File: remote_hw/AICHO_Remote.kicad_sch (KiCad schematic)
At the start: 25 parts, among them J1 Conn_01x04, J2 Conn_01x03_Pin, J3 RJ45, U1 TPS54302, U3 PY32F003F18U6, U4 SP485E, Y1 16MHz 9pF

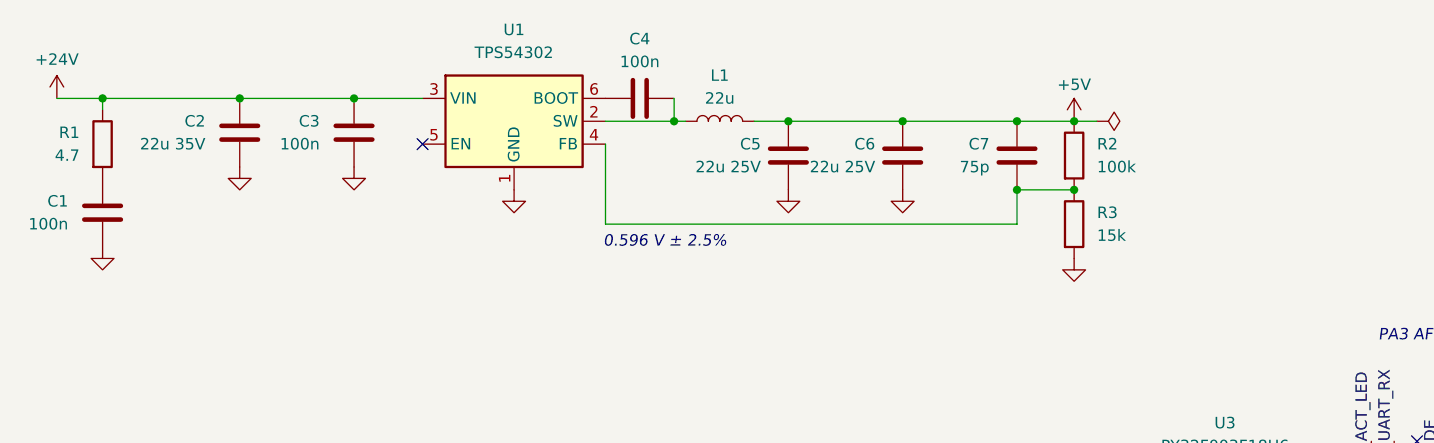
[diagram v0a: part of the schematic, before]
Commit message: remote_hw: Change DC-DC input capacitors to 10 uF * 2
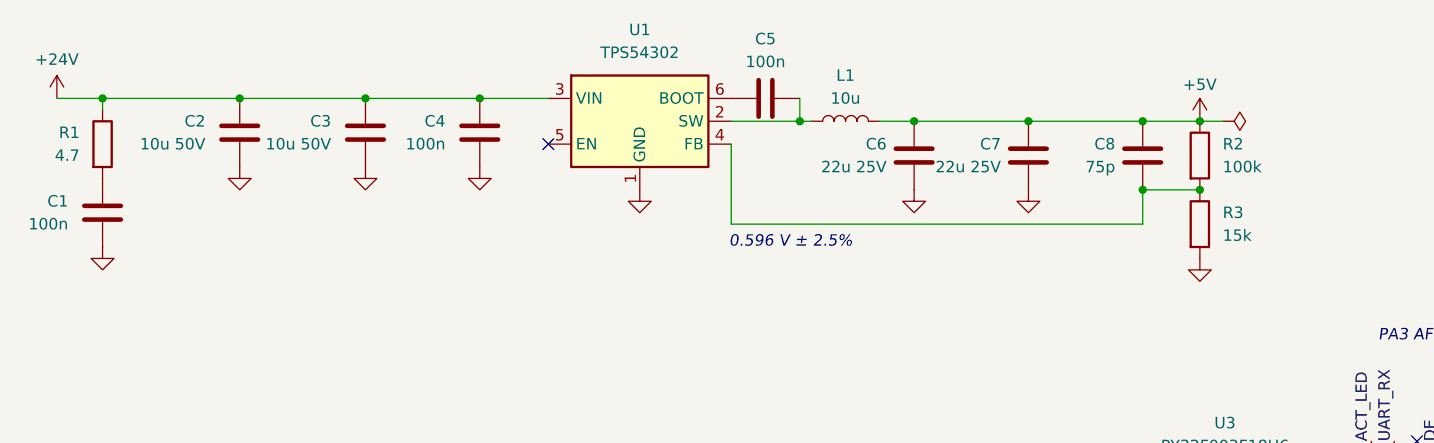
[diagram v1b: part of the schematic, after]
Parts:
- added C3: 10u 50V, Capacitor_SMD:C_0805_2012Metric, symbol Device:C
- C2: value 22u 35V -> 10u 50V; footprint Capacitor_SMD:C_1210_3225Metric -> Capacitor_SMD:C_0805_2012Metric; LCSC PN C778721 -> C338080; Mfr PN (none) -> C2012X5R1V226MT000E
- L1: value 22u -> 10u; footprint Inductor_SMD:L_Sunlord_SWPA6045S -> Inductor_SMD:L_Sunlord_SWPA4030S; LCSC PN C83454 -> C38117; Mfr PN SWPA6045S220MT -> SWPA4030S100MT
- renumbered C3 to C4, C4 to C5, C5 to C6, C6 to C7, C7 to C8
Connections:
- net +24V: now also C3.1
- net GND: now also C3.2
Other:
- moved on the sheet: C4, C5, C6, C7, C8, L1, R2, R3, U1

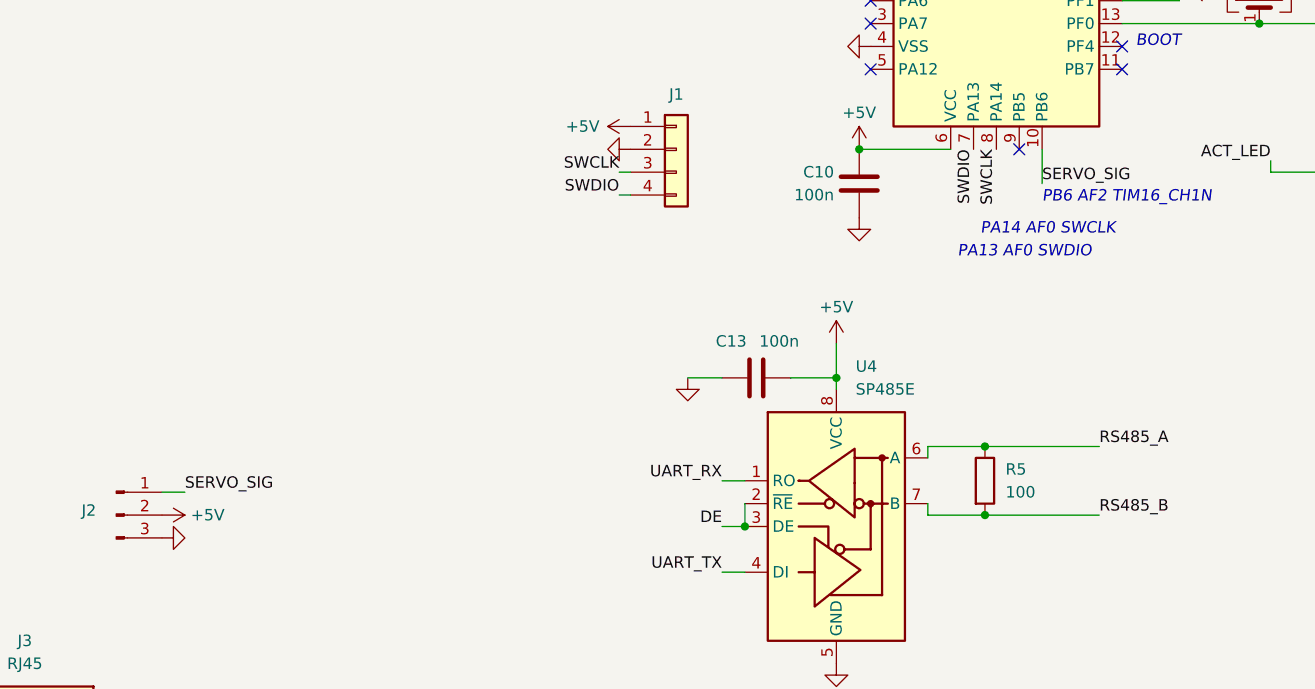
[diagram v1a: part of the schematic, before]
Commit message: remote_hw: Lay out DC-DC
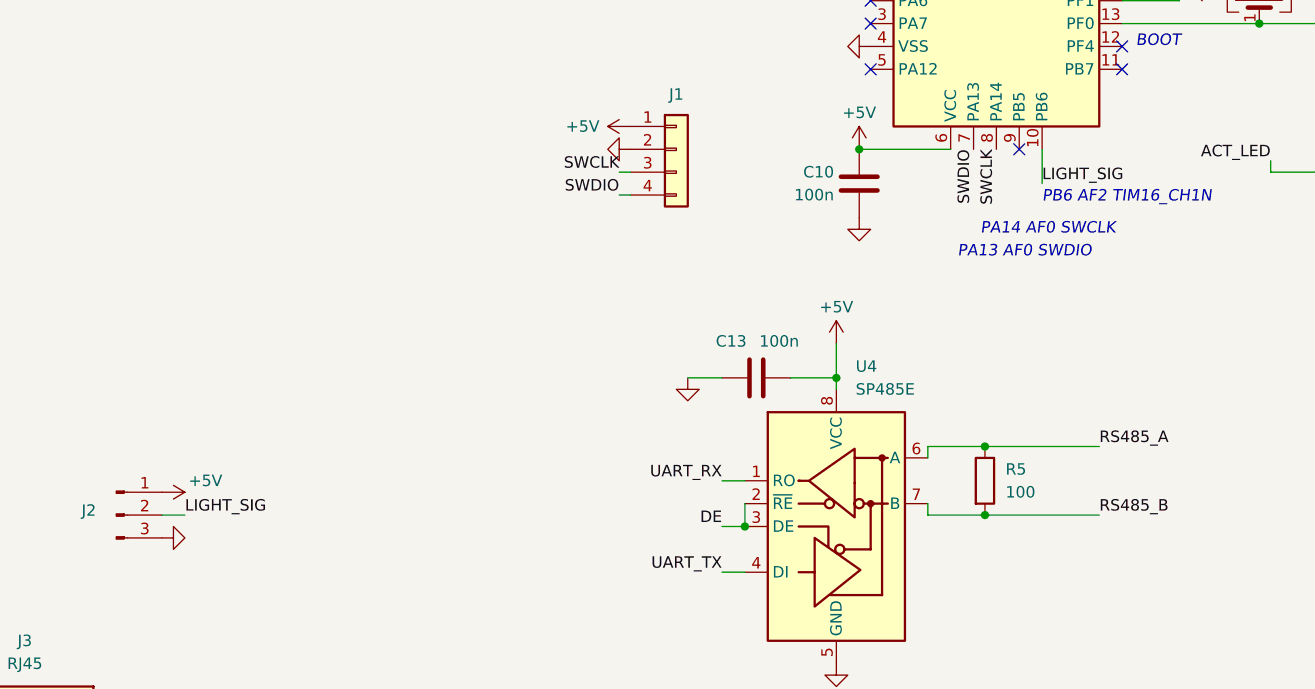
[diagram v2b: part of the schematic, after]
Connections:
- net +5V: now also J2.1 (Pin_1); no longer J2.2 (Pin_2)
- net SERVO_SIG renamed LIGHT_SIG
- net LIGHT_SIG: now also J2.2 (Pin_2); no longer J2.1 (Pin_1)
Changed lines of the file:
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@@
 	(wire
 		(pts
-			(xy 85.09 133.35) (xy 82.55 133.35)
+			(xy 85.09 135.89) (xy 82.55 135.89)
 		)
 		(stroke
@@
 		)
 	)
-	(label "SERVO_SIG"
-		(at 85.09 133.35 0)
+	(label "LIGHT_SIG"
+		(at 85.09 135.89 0)
 		(effects
 			(font
@@
 		)
 	)
-	(label "SERVO_SIG"
+	(label "LIGHT_SIG"
 		(at 180.34 99.06 0)
 		(effects
@@
 	(symbol
 		(lib_id "power:+5V")
-		(at 82.55 135.89 270)
+		(at 82.55 133.35 270)
 		(unit 1)
 		(exclude_from_sim no)
@@
 		(dnp no)
 		(property "Reference" "#PWR016"
-			(at 78.74 135.89 0)
+			(at 78.74 133.35 0)
 			(effects
 				(font
@@
 		)
 		(property "Value" "+5V"
-			(at 87.63 135.89 90)
+			(at 87.376 132.08 90)
 			(effects
 				(font
@@
 		)
 		(property "Footprint" ""
-			(at 82.55 135.89 0)
+			(at 82.55 133.35 0)
 			(effects
 				(font
@@
 		)
 		(property "Datasheet" ""
-			(at 82.55 135.89 0)
+			(at 82.55 133.35 0)
 			(effects
 				(font
@@
 		)
 		(property "Description" "Power symbol creates a global label with name \"+5V\""
-			(at 82.55 135.89 0)
-			(effects
-				(font
+			(at 82.55 133.35 0)
+			(effects
+				(font

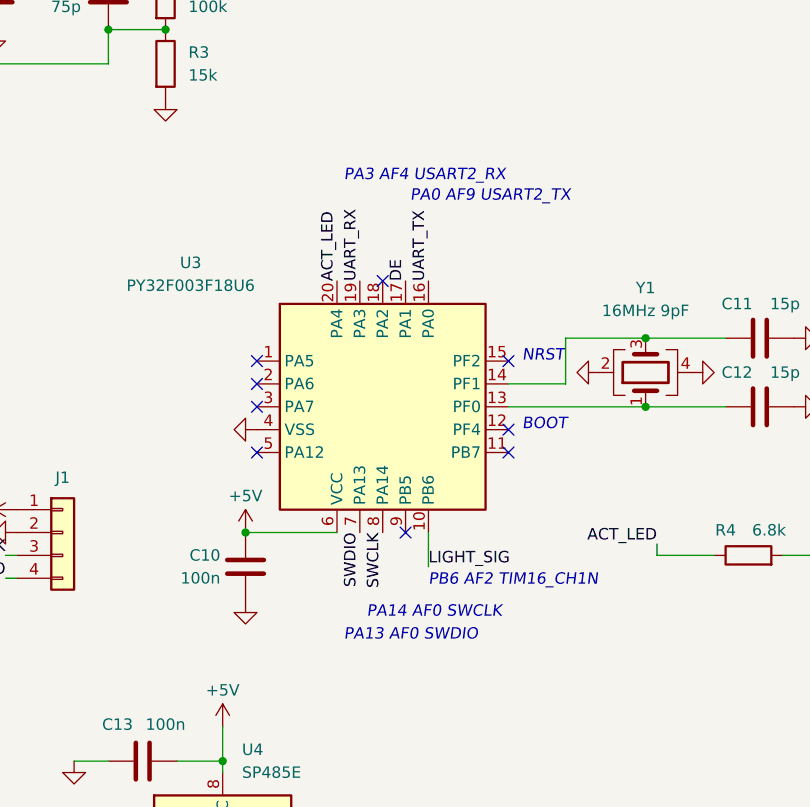
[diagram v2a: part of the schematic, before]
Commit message: remote_hw: Finish layout & routing
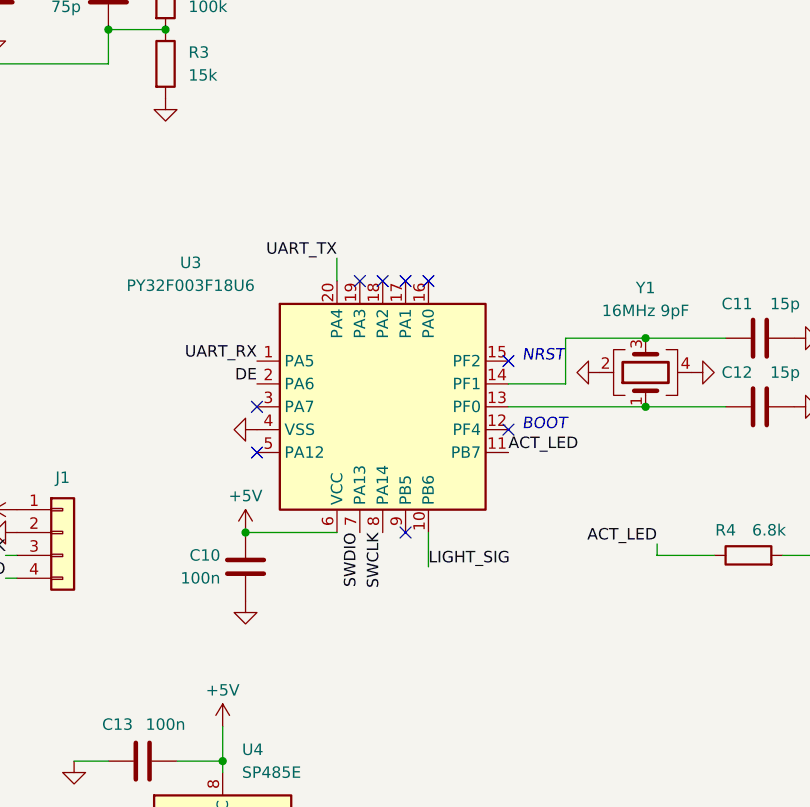
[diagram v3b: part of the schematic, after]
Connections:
- net ACT_LED: now also U3.11 (PB7); no longer U3.20 (PA4)
- net DE: now also U3.2 (PA6); no longer U3.17 (PA1)
- net UART_RX: now also U3.1 (PA5); no longer U3.19 (PA3)
- net UART_TX: now also U3.20 (PA4); no longer U3.16 (PA0)
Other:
- note removed: "PA0 AF9 USART2_TX"
- note removed: "PA13 AF0 SWDIO"
- note removed: "PA14 AF0 SWCLK"
- note removed: "PA3 AF4 USART2_RX"
- note removed: "PB6 AF2 TIM16_CH1N"
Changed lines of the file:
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@@
 	(generator_version "9.0")
 	(paper "A4")
-	(text "PA0 AF9 USART2_TX"
-		(exclude_from_sim no)
-		(at 178.308 58.674 0)
-		(effects
-			(font
-				(size 1.27 1.27)
-				(italic yes)
-			)
-			(justify left bottom)
-		)
-	)
 	(text "BOOT"
 		(exclude_from_sim no)
@@
 		)
 	)
-	(text "PA3 AF4 USART2_RX"
-		(exclude_from_sim no)
-		(at 170.942 56.388 0)
-		(effects
-			(font
-				(size 1.27 1.27)
-				(italic yes)
-			)
-			(justify left bottom)
-		)
-	)
 	(text "0.596 V ± 2.5%"
 		(exclude_from_sim no)
@@
 		)
 	)
-	(text "PA14 AF0 SWCLK"
-		(exclude_from_sim no)
-		(at 173.482 104.902 0)
-		(effects
-			(font
-				(size 1.27 1.27)
-				(italic yes)
-			)
-			(justify left bottom)
-		)
-	)
-	(text "PA13 AF0 SWDIO"
-		(exclude_from_sim no)
-		(at 170.942 107.442 0)
-		(effects
-			(font
-				(size 1.27 1.27)
-				(italic yes)
-			)
-			(justify left bottom)
-		)
-	)
-	(text "PB6 AF2 TIM16_CH1N"
-		(exclude_from_sim no)
-		(at 180.34 101.346 0)
-		(effects
-			(font
-				(size 1.27 1.27)
-				(italic yes)
-			)
-			(justify left bottom)
-		)
-	)
 	(junction
 		(at 29.21 29.21)
@@
 	)
 	(no_connect
+		(at 177.8 67.31)
+	)
+	(no_connect
 		(at 161.29 86.36)
 	)
@@
 	)
 	(no_connect
-		(at 189.23 86.36)
-	)
-	(no_connect
-		(at 161.29 78.74)
-	)
-	(no_connect
 		(at 78.74 34.29)
 	)
 	(no_connect
-		(at 161.29 76.2)
-	)
-	(no_connect
 		(at 161.29 81.28)
 	)
@@
 		(at 189.23 83.82)
 	)
+	(no_connect
+		(at 180.34 67.31)
+	)
+	(no_connect
+		(at 172.72 67.31)
+	)
 	(wire
 		(pts
@@
 		(pts
 			(xy 219.71 97.79) (xy 223.52 97.79)
+		)
+		(stroke
+			(width 0)
+			(type default)
+		)
+	)
+	(wire
+		(pts
+			(xy 170.18 64.77) (xy 170.18 67.31)
 		)
 		(stroke
@@
 		)
 	)
-	(label "UART_RX"
-		(at 172.72 67.31 90)
-		(effects
-			(font
-				(size 1.27 1.27)
-			)
-			(justify left bottom)
-		)
-	)
 	(label "SWDIO"
 		(at 172.72 95.25 270)
@@
 		)
 	)
-	(label "UART_TX"
-		(at 180.34 67.31 90)
-		(effects
-			(font
-				(size 1.27 1.27)
-			)
-			(justify left bottom)
-		)
-	)
 	(label "SWDIO"
 		(at 133.35 100.33 180)
@@
 		)
 	)
+	(label "DE"
+		(at 161.29 78.74 180)
+		(effects
+			(font
+				(size 1.27 1.27)
+			)
+			(justify right bottom)
+		)
+	)
 	(label "ACT_LED"
 		(at 205.74 96.52 180)
@@
 		)
 	)
+	(label "ACT_LED"
+		(at 189.23 86.36 0)
+		(effects
+			(font
+				(size 1.27 1.27)
+			)
+			(justify left bottom)
+		)
+	)
+	(label "UART_RX"
+		(at 161.29 76.2 180)
+		(effects
+			(font
+				(size 1.27 1.27)
+			)
+			(justify right bottom)
+		)
+	)
+	(label "RS485_B"
+		(at 186.69 135.89 0)
+		(effects
+			(font
+				(size 1.27 1.27)
+			)
+			(justify left bottom)
+		)
+	)
+	(label "UART_TX"
+		(at 144.78 142.24 180)
+		(effects
+			(font
+				(size 1.27 1.27)
+			)
+			(justify right bottom)
+		)
+	)
+	(label "SWCLK"
+		(at 133.35 97.79 180)
+		(effects
+			(font
+				(size 1.27 1.27)
+			)
+			(justify right bottom)
+		)
+	)
+	(label "UART_TX"
+		(at 170.18 64.77 180)
+		(effects
+			(font
+				(size 1.27 1.27)
+			)
+			(justify right bottom)
+		)
+	)
+	(label "SWCLK"
+		(at 175.26 95.25 270)
+		(effects
+			(font
+				(size 1.27 1.27)
+			)
+			(justify right bottom)
+		)
+	)
+	(label "RS485_B"
+		(at 80.01 172.72 0)
+		(effects
+			(font
+				(size 1.27 1.27)
+			)
+			(justify left bottom)
+		)
+	)
 	(label "LIGHT_SIG"
 		(at 180.34 99.06 0)
 		(effects
 			(font
-				(size 1.27 1.27)
-			)
-			(justify left bottom)
-		)
-	)
-	(label "RS485_B"
-		(at 186.69 135.89 0)
-		(effects
-			(font
-				(size 1.27 1.27)
-			)
-			(justify left bottom)
-		)
-	)
-	(label "UART_TX"
-		(at 144.78 142.24 180)
-		(effects
-			(font
-				(size 1.27 1.27)
-			)
-			(justify right bottom)
-		)
-	)
-	(label "DE"
-		(at 177.8 67.31 90)
-		(effects
-			(font
-				(size 1.27 1.27)
-			)
-			(justify left bottom)
-		)
-	)
-	(label "ACT_LED"
-		(at 170.18 67.31 90)
-		(effects
-			(font
-				(size 1.27 1.27)
-			)
-			(justify left bottom)
-		)
-	)
-	(label "SWCLK"
-		(at 133.35 97.79 180)
-		(effects
-			(font
-				(size 1.27 1.27)
-			)
-			(justify right bottom)
-		)
-	)
-	(label "SWCLK"
-		(at 175.26 95.25 270)
-		(effects
-			(font
-				(size 1.27 1.27)
-			)
-			(justify right bottom)
-		)
-	)
-	(label "RS485_B"
-		(at 80.01 172.72 0)
-		(effects
-			(font

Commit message: remote_hw: Revise details
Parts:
- renumbered U3 to U2, U4 to U3
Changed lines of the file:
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@@
 		(on_board yes)
 		(dnp no)
-		(property "Reference" "U3"
+		(property "Reference" "U2"
 			(at 153.924 65.278 0)
 			(effects
@@
 			(project ""
 				(path "/6c51c4e7-714d-4ba2-b183-a9bbda12c420"
-					(reference "U3")
+					(reference "U2")
 					(unit 1)
 				)
@@
 		(dnp no)
 		(fields_autoplaced yes)
-		(property "Reference" "U4"
+		(property "Reference" "U3"
 			(at 159.6233 119.38 0)
 			(effects
@@
 			(project ""
 				(path "/6c51c4e7-714d-4ba2-b183-a9bbda12c420"
-					(reference "U4")
-					(unit 1)
-				)
+					(reference "U3")
+					(unit 1)
+				)

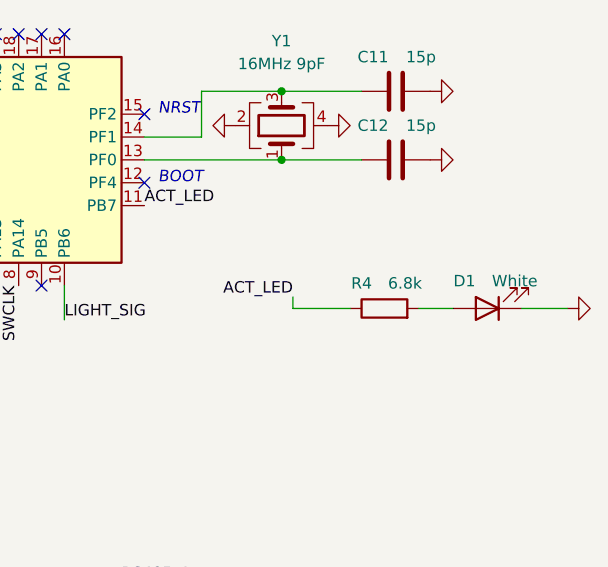
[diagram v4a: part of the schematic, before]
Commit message: remote_hw: Update component values with fabrication settings
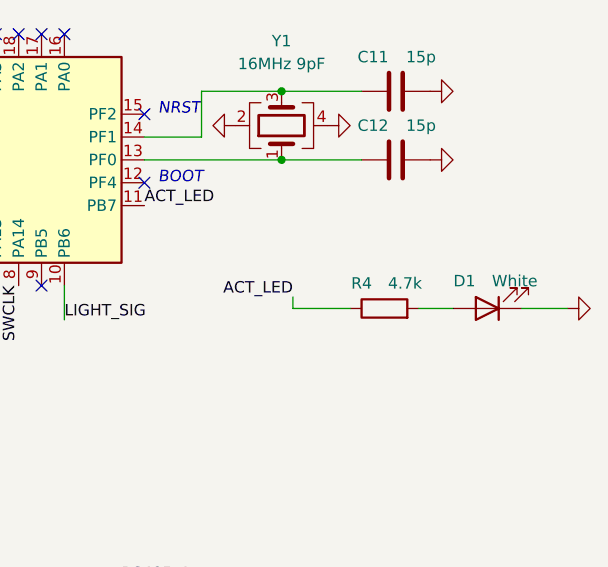
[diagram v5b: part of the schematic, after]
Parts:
- C2, C3: LCSC PN C338080 -> (none); Mfr PN C2012X5R1V226MT000E -> (none)
- R4: value 6.8k -> 4.7k
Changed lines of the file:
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@@
 			)
 		)
-		(property "Value" "6.8k"
+		(property "Value" "4.7k"
 			(at 218.186 94.996 90)
 			(effects
@@
 			)
 		)
-		(property "LCSC PN" "C338080"
-			(at 58.42 33.02 0)
-			(effects
-				(font
-					(size 1.27 1.27)
-				)
-				(hide yes)
-			)
-		)
-		(property "Mfr PN" "C2012X5R1V226MT000E"
-			(at 58.42 33.02 0)
-			(effects
-				(font
-					(size 1.27 1.27)
-				)
-				(hide yes)
-			)
-		)
 		(pin "2"
 		)
@@
 			(at 44.45 33.02 0)
 			(effects
-				(font
-					(size 1.27 1.27)
-				)
-				(hide yes)
-			)
-		)
-		(property "LCSC PN" "C338080"
-			(at 44.45 33.02 0)
-			(effects
-				(font
-					(size 1.27 1.27)
-				)
-				(hide yes)
-			)
-		)
-		(property "Mfr PN" "C2012X5R1V226MT000E"
-			(at 44.45 33.02 0)
-			(effects
